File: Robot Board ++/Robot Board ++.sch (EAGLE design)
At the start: 124 parts, among them U10 74XX125.RGY, U11 SCHA4B0400, U12 BLUETOOTH-RN41", U13 XBEE-1XBEE-1_LOCK, U5 TPS5331[8/9].DQP, U6 TPS62082.DSG, U7 PCA9557.RGV, U8 MPU-6050

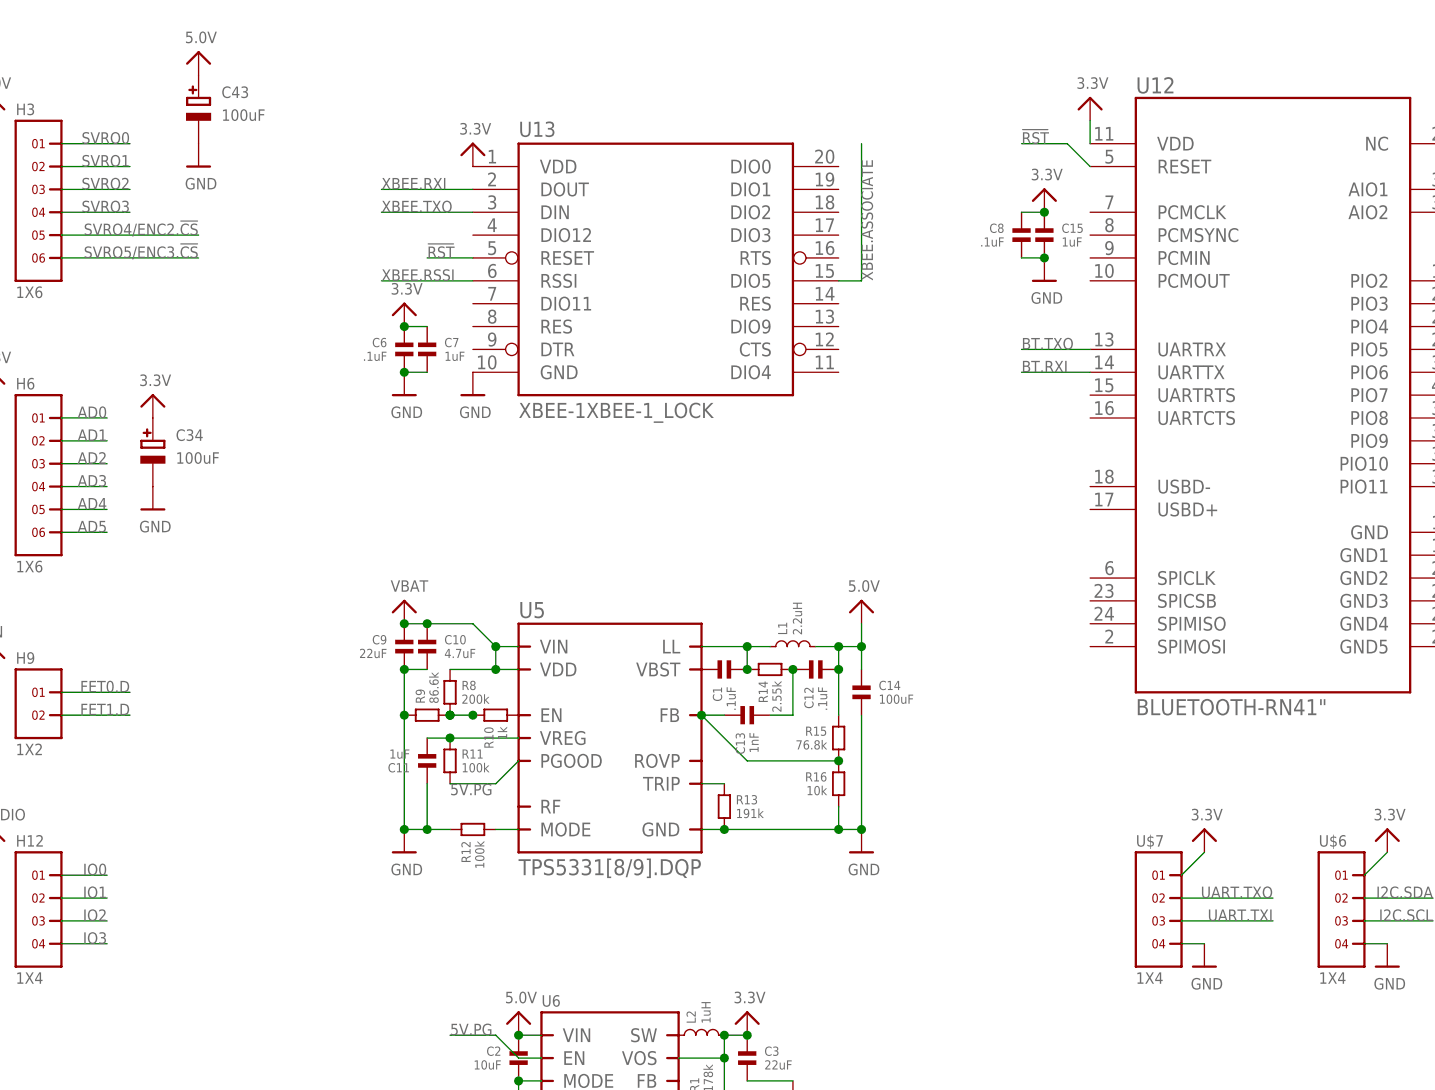
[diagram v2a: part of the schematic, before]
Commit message: Added I2C and UART headers Connected most signals on PCB  Will need to clean up...
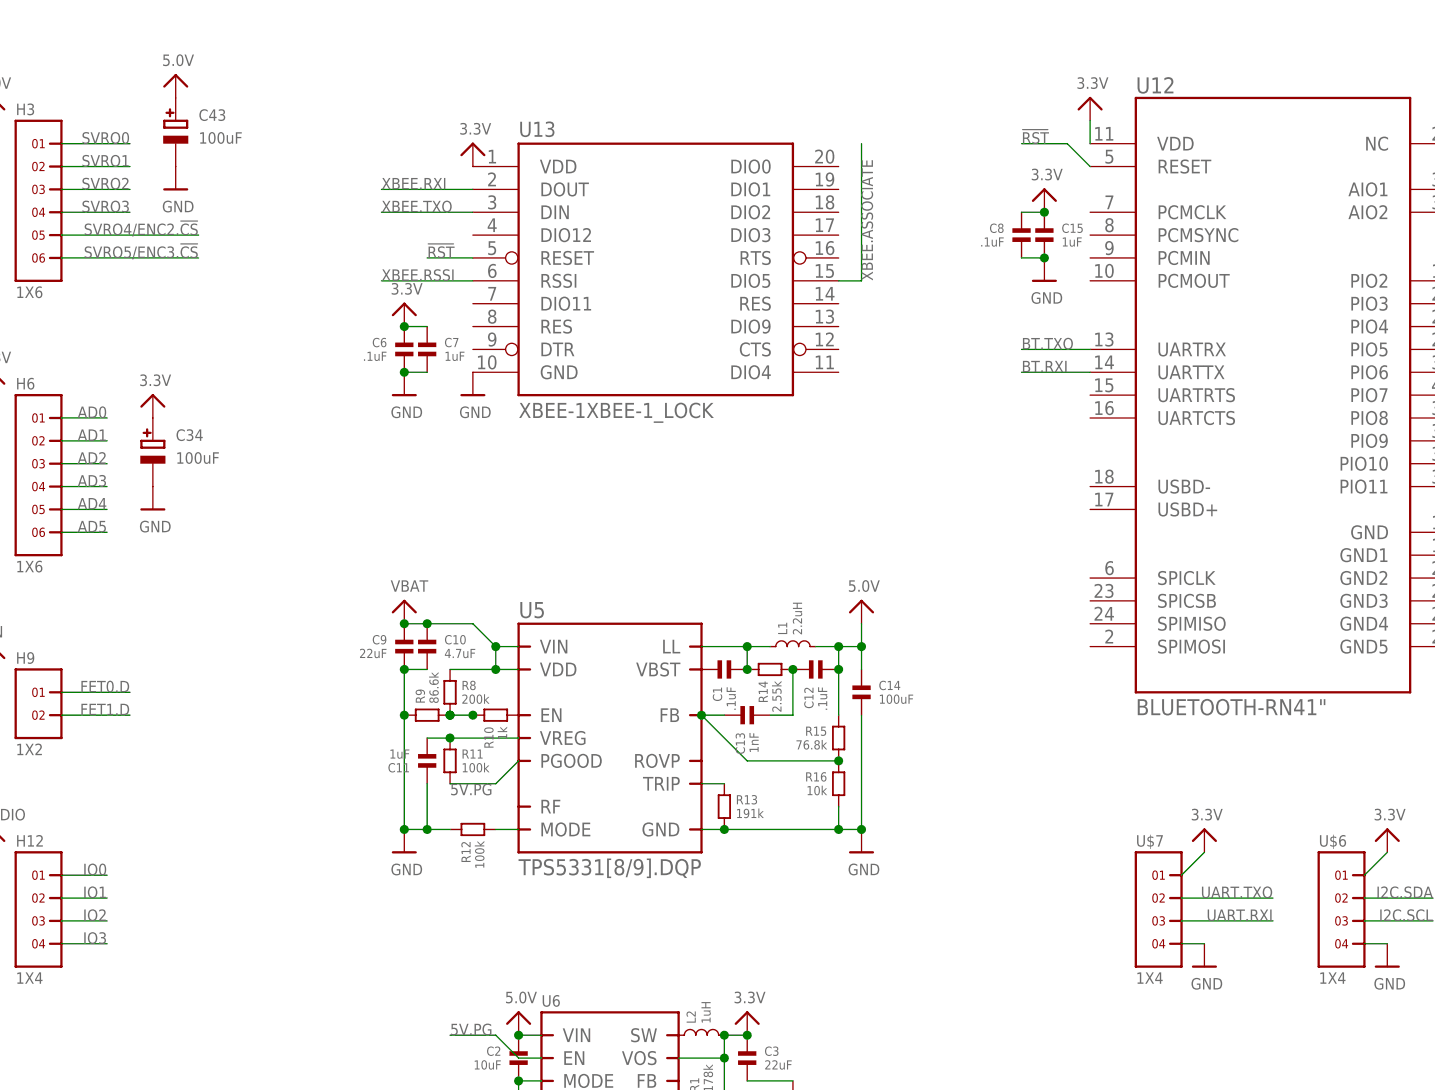
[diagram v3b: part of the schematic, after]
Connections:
- removed net UART.TXI: U$7.3
- net UART.RXI: now also U$7.3
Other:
- moved on the sheet: C43
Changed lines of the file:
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@@
 <instance part="U$138" gate="G$1" x="180.34" y="15.24"/>
 <instance part="U$1" gate="G$1" x="312.42" y="96.52"/>
-<instance part="C43" gate="G$1" x="48.26" y="241.3"/>
-<instance part="U$2" gate="G$1" x="48.26" y="248.92"/>
-<instance part="U$5" gate="G$1" x="48.26" y="236.22"/>
+<instance part="C43" gate="G$1" x="45.72" y="238.76"/>
+<instance part="U$2" gate="G$1" x="45.72" y="246.38"/>
+<instance part="U$5" gate="G$1" x="45.72" y="233.68"/>
 <instance part="U$6" gate="G$1" x="175.26" y="152.4"/>
 <instance part="U$7" gate="G$1" x="154.94" y="152.4"/>
@@
 <label x="289.56" y="195.58" size="1.27" layer="95"/>
 </segment>
+<segment>
+<pinref part="U$7" gate="G$1" pin="3"/>
+<wire x1="167.64" y1="152.4" x2="157.48" y2="152.4" width="0.1524" layer="91"/>
+<label x="167.64" y="152.4" size="1.27" layer="95" rot="MR0"/>
+</segment>
 </net>
 <net name="UART.TXO" class="0">
@@
 </segment>
 </net>
-<net name="UART.TXI" class="0">
-<segment>
-<pinref part="U$7" gate="G$1" pin="3"/>
-<wire x1="167.64" y1="152.4" x2="157.48" y2="152.4" width="0.1524" layer="91"/>
-<label x="167.64" y="152.4" size="1.27" layer="95" rot="MR0"/>
-</segment>
-</net>

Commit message: most power lines routed
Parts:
- removed H25: 1X3, headers(2mm):1X3
- H27: value 1X3 -> 1X2; device headers(2mm):1X3 -> headers(.1in):1X2
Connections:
- net 3.3V: now also H11.1, H11.2, H11.3, H11.4, H13.1, H14.1, H15.1, H16.1; no longer H25.1
- net 5.0V: no longer H25.3, H27.1
- net VBAT: now also H27.2; no longer H27.3
- net VDDIO: no longer H11.1, H11.2, H11.3, H11.4, H13.1, H14.1, H15.1, H16.1, H25.2
- net VIN: now also H27.1; no longer H27.2
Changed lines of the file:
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@@
 <part name="U$72" library="microbuilder" deviceset="3.3V" device=""/>
 <part name="U$74" library="microbuilder" deviceset="GND" device=""/>
-<part name="H25" library="headers(2mm)" deviceset="1X3" device=""/>
-<part name="H27" library="headers(2mm)" deviceset="1X3" device=""/>
-<part name="U$77" library="microbuilder" deviceset="3.3V" device=""/>
-<part name="U$79" library="microbuilder" deviceset="5.0V" device=""/>
-<part name="U$81" library="microbuilder" deviceset="5.0V" device=""/>
+<part name="H27" library="headers(.1in)" deviceset="1X2" device=""/>
 <part name="U$82" library="microbuilder" deviceset="VBAT" device=""/>
 <part name="U$84" library="microbuilder" deviceset="VBAT" device=""/>
@@
 <part name="U$87" library="microbuilder" deviceset="VBAT" device=""/>
 <part name="U$88" library="microbuilder" deviceset="3.3V" device=""/>
-<part name="U$89" library="microbuilder" deviceset="VDDIO" device=""/>
-<part name="U$90" library="microbuilder" deviceset="VDDIO" device=""/>
-<part name="U$51" library="microbuilder" deviceset="VDDIO" device=""/>
-<part name="U$52" library="microbuilder" deviceset="VDDIO" device=""/>
-<part name="U$53" library="microbuilder" deviceset="VDDIO" device=""/>
-<part name="U$54" library="microbuilder" deviceset="VDDIO" device=""/>
 <part name="U$91" library="microbuilder" deviceset="VIN" device=""/>
 <part name="U$92" library="microbuilder" deviceset="VIN" device=""/>
@@
 <part name="U$32" library="microbuilder" deviceset="GND" device=""/>
 <part name="U$30" library="microbuilder" deviceset="3.3V" device=""/>
+<part name="U$33" library="microbuilder" deviceset="3.3V" device=""/>
+<part name="U$35" library="microbuilder" deviceset="3.3V" device=""/>
+<part name="U$36" library="microbuilder" deviceset="3.3V" device=""/>
+<part name="U$37" library="microbuilder" deviceset="3.3V" device=""/>
+<part name="U$38" library="microbuilder" deviceset="3.3V" device=""/>
 </parts>
 <sheets>
@@
 <instance part="U$72" gate="G$1" x="147.32" y="243.84"/>
 <instance part="U$74" gate="G$1" x="205.74" y="208.28"/>
-<instance part="H25" gate="G$1" x="309.88" y="55.88"/>
 <instance part="H27" gate="G$1" x="350.52" y="55.88"/>
-<instance part="U$77" gate="G$1" x="314.96" y="58.42" rot="R270"/>
-<instance part="U$79" gate="G$1" x="314.96" y="53.34" rot="R270"/>
-<instance part="U$81" gate="G$1" x="355.6" y="58.42" rot="R270"/>
 <instance part="U$82" gate="G$1" x="355.6" y="53.34" rot="R270"/>
 <instance part="U$84" gate="G$1" x="55.88" y="68.58" rot="MR0"/>
@@
 <instance part="U$87" gate="G$1" x="71.12" y="68.58"/>
 <instance part="U$88" gate="G$1" x="228.6" y="124.46"/>
-<instance part="U$89" gate="G$1" x="320.04" y="60.96"/>
-<instance part="U$90" gate="G$1" x="25.4" y="162.56"/>
-<instance part="U$51" gate="G$1" x="22.86" y="114.3"/>
-<instance part="U$52" gate="G$1" x="22.86" y="96.52"/>
-<instance part="U$53" gate="G$1" x="63.5" y="96.52"/>
-<instance part="U$54" gate="G$1" x="63.5" y="114.3"/>
-<instance part="U$91" gate="G$1" x="360.68" y="60.96"/>
+<instance part="U$91" gate="G$1" x="355.6" y="58.42"/>
 <instance part="U$92" gate="G$1" x="25.4" y="182.88"/>
 <instance part="U$20" gate="G$1" x="109.22" y="142.24"/>
@@
 <instance part="U$32" gate="G$1" x="43.18" y="198.12"/>
 <instance part="U$30" gate="G$1" x="43.18" y="210.82"/>
+<instance part="U$33" gate="G$1" x="25.4" y="162.56"/>
+<instance part="U$35" gate="G$1" x="22.86" y="114.3"/>
+<instance part="U$36" gate="G$1" x="22.86" y="96.52"/>
+<instance part="U$37" gate="G$1" x="63.5" y="96.52"/>
+<instance part="U$38" gate="G$1" x="63.5" y="114.3"/>
 </instances>
 <busses>
@@
 <net name="3.3V" class="0">
 <segment>
-<pinref part="H25" gate="G$1" pin="1"/>
-<pinref part="U$77" gate="G$1" pin="3.3V"/>
-</segment>
-<segment>
 <pinref part="C3" gate="G$1" pin="1"/>
 <pinref part="U$20" gate="G$1" pin="3.3V"/>
@@
 <pinref part="U$30" gate="G$1" pin="3.3V"/>
 </segment>
+<segment>
+<pinref part="H11" gate="G$1" pin="4"/>
+<wire x1="25.4" y1="149.86" x2="25.4" y2="152.4" width="0.1524" layer="91"/>
+<pinref part="H11" gate="G$1" pin="3"/>
+<junction x="25.4" y="152.4"/>
+<wire x1="25.4" y1="152.4" x2="25.4" y2="154.94" width="0.1524" layer="91"/>
+<pinref part="H11" gate="G$1" pin="2"/>
+<junction x="25.4" y="154.94"/>
+<wire x1="25.4" y1="154.94" x2="25.4" y2="157.48" width="0.1524" layer="91"/>
+<pinref part="H11" gate="G$1" pin="1"/>
+<junction x="25.4" y="157.48"/>
+<wire x1="25.4" y1="157.48" x2="25.4" y2="160.02" width="0.1524" layer="91"/>
+<pinref part="U$33" gate="G$1" pin="3.3V"/>
+</segment>
+<segment>
+<pinref part="H13" gate="G$1" pin="1"/>
+<wire x1="22.86" y1="111.76" x2="25.4" y2="109.22" width="0.1524" layer="91"/>
+<pinref part="U$35" gate="G$1" pin="3.3V"/>
+</segment>
+<segment>
+<pinref part="H14" gate="G$1" pin="1"/>
+<wire x1="22.86" y1="93.98" x2="25.4" y2="91.44" width="0.1524" layer="91"/>
+<pinref part="U$36" gate="G$1" pin="3.3V"/>
+</segment>
+<segment>
+<pinref part="H16" gate="G$1" pin="1"/>
+<wire x1="63.5" y1="93.98" x2="66.04" y2="91.44" width="0.1524" layer="91"/>
+<pinref part="U$37" gate="G$1" pin="3.3V"/>
+</segment>
+<segment>
+<pinref part="H15" gate="G$1" pin="1"/>
+<wire x1="63.5" y1="111.76" x2="66.04" y2="109.22" width="0.1524" layer="91"/>
+<pinref part="U$38" gate="G$1" pin="3.3V"/>
+</segment>
 </net>
 <net name="SVRO0" class="0">
@@
 <segment>
 <pinref part="U7" gate="G$1" pin="P4"/>
-<wire x1="177.8" y1="86.36" x2="182.88" y2="86.36" width="0.1524" layer="91"/>
-<label x="182.88" y="86.36" size="1.27" layer="95" rot="MR0"/>
+<wire x1="177.8" y1="86.36" x2="185.42" y2="86.36" width="0.1524" layer="91"/>
+<label x="185.42" y="86.36" size="1.27" layer="95" rot="MR0"/>
 </segment>
 </net>
@@
 <segment>
 <pinref part="U7" gate="G$1" pin="P5"/>
-<wire x1="177.8" y1="83.82" x2="182.88" y2="83.82" width="0.1524" layer="91"/>
-<label x="182.88" y="83.82" size="1.27" layer="95" rot="MR0"/>
+<wire x1="177.8" y1="83.82" x2="185.42" y2="83.82" width="0.1524" layer="91"/>
+<label x="185.42" y="83.82" size="1.27" layer="95" rot="MR0"/>
 </segment>
 </net>
@@
 </segment>
 <segment>
-<pinref part="H25" gate="G$1" pin="3"/>
-<pinref part="U$79" gate="G$1" pin="5.0V"/>
-</segment>
-<segment>
-<pinref part="H27" gate="G$1" pin="1"/>
-<pinref part="U$81" gate="G$1" pin="5.0V"/>
-</segment>
-<segment>
 <pinref part="L1" gate="G$1" pin="2"/>
 <wire x1="116.84" y1="182.88" x2="119.38" y2="182.88" width="0.1524" layer="91"/>
@@
 <net name="VBAT" class="0">
 <segment>
-<pinref part="H27" gate="G$1" pin="3"/>
+<pinref part="H27" gate="G$1" pin="2"/>
 <pinref part="U$82" gate="G$1" pin="VBAT"/>
 </segment>
@@
 <net name="VDDIO" class="0">
 <segment>
-<pinref part="H25" gate="G$1" pin="2"/>
-<wire x1="312.42" y1="55.88" x2="320.04" y2="55.88" width="0.1524" layer="91"/>
-<pinref part="U$89" gate="G$1" pin="VDDIO"/>
-<wire x1="320.04" y1="55.88" x2="320.04" y2="58.42" width="0.1524" layer="91"/>
-</segment>
-<segment>
-<pinref part="U$90" gate="G$1" pin="VDDIO"/>
-<pinref part="H11" gate="G$1" pin="4"/>
-<wire x1="25.4" y1="149.86" x2="25.4" y2="152.4" width="0.1524" layer="91"/>
-<pinref part="H11" gate="G$1" pin="3"/>
-<junction x="25.4" y="152.4"/>
-<wire x1="25.4" y1="152.4" x2="25.4" y2="154.94" width="0.1524" layer="91"/>
-<pinref part="H11" gate="G$1" pin="2"/>
-<junction x="25.4" y="154.94"/>
-<wire x1="25.4" y1="154.94" x2="25.4" y2="157.48" width="0.1524" layer="91"/>
-<pinref part="H11" gate="G$1" pin="1"/>
-<junction x="25.4" y="157.48"/>
-<wire x1="25.4" y1="157.48" x2="25.4" y2="160.02" width="0.1524" layer="91"/>
-</segment>
-<segment>
-<pinref part="H13" gate="G$1" pin="1"/>
-<pinref part="U$51" gate="G$1" pin="VDDIO"/>
-<wire x1="22.86" y1="111.76" x2="25.4" y2="109.22" width="0.1524" layer="91"/>
-</segment>
-<segment>
-<pinref part="H14" gate="G$1" pin="1"/>
-<pinref part="U$52" gate="G$1" pin="VDDIO"/>
-<wire x1="22.86" y1="93.98" x2="25.4" y2="91.44" width="0.1524" layer="91"/>
-</segment>
-<segment>
-<pinref part="H16" gate="G$1" pin="1"/>
-<pinref part="U$53" gate="G$1" pin="VDDIO"/>
-<wire x1="63.5" y1="93.98" x2="66.04" y2="91.44" width="0.1524" layer="91"/>
-</segment>
-<segment>
-<pinref part="H15" gate="G$1" pin="1"/>
-<pinref part="U$54" gate="G$1" pin="VDDIO"/>
-<wire x1="63.5" y1="111.76" x2="66.04" y2="109.22" width="0.1524" layer="91"/>
-</segment>
-<segment>
 <pinref part="R5" gate="G$1" pin="1"/>
 <pinref part="U$58" gate="G$1" pin="VDDIO"/>
@@
 </segment>
 <segment>
-<pinref part="H27" gate="G$1" pin="2"/>
-<wire x1="353.06" y1="55.88" x2="360.68" y2="55.88" width="0.1524" layer="91"/>
+<pinref part="H27" gate="G$1" pin="1"/>
+<wire x1="353.06" y1="55.88" x2="355.6" y2="55.88" width="0.1524" layer="91"/>
 <pinref part="U$91" gate="G$1" pin="VIN"/>
-<wire x1="360.68" y1="58.42" x2="360.68" y2="55.88" width="0.1524" layer="91"/>
-</segment>
-</net>
+</segment>
+</net>

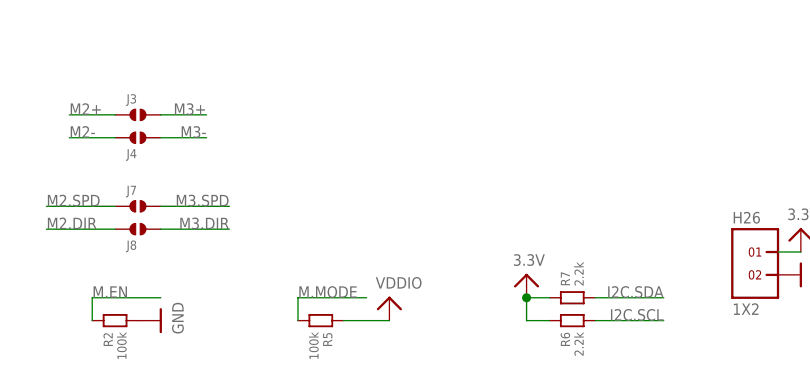
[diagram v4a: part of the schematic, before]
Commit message: More routing. Most motor control signals completed. Successfully making larger ground plane.
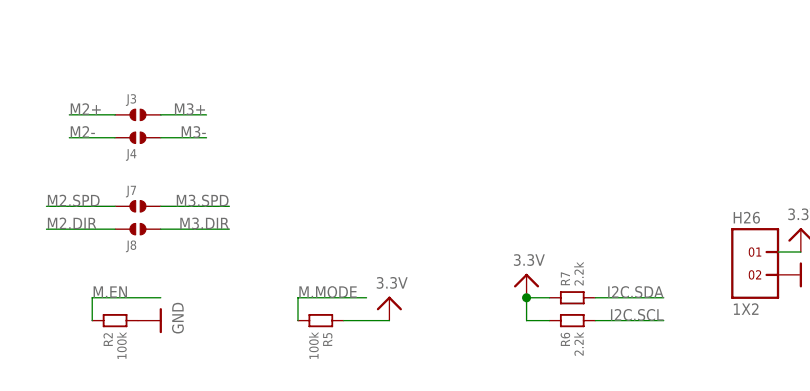
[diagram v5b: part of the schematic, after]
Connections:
- removed net VDDIO: R5.1
- net 3.3V: now also R5.1
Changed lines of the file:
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@@
 <part name="U$56" library="microbuilder" deviceset="GND" device=""/>
 <part name="R5" library="standardparts" deviceset="RESISTOR" device=".0603" value="100k"/>
-<part name="U$58" library="microbuilder" deviceset="VDDIO" device=""/>
 <part name="U$111" library="microbuilder" deviceset="3.3V" device=""/>
 <part name="U$137" library="microbuilder" deviceset="GND" device=""/>
@@
 <part name="U$37" library="microbuilder" deviceset="3.3V" device=""/>
 <part name="U$38" library="microbuilder" deviceset="3.3V" device=""/>
+<part name="U$39" library="microbuilder" deviceset="3.3V" device=""/>
 </parts>
 <sheets>
@@
 <instance part="U$56" gate="G$1" x="347.98" y="88.9"/>
 <instance part="R5" gate="G$1" x="157.48" y="10.16" rot="R180"/>
-<instance part="U$58" gate="G$1" x="165.1" y="12.7"/>
 <instance part="U$111" gate="G$1" x="340.36" y="198.12"/>
 <instance part="U$137" gate="G$1" x="340.36" y="187.96"/>
@@
 <instance part="U$37" gate="G$1" x="63.5" y="96.52"/>
 <instance part="U$38" gate="G$1" x="63.5" y="114.3"/>
+<instance part="U$39" gate="G$1" x="165.1" y="12.7"/>
 </instances>
 <busses>
@@
 <pinref part="U$38" gate="G$1" pin="3.3V"/>
 </segment>
+<segment>
+<pinref part="R5" gate="G$1" pin="1"/>
+<wire x1="160.02" y1="10.16" x2="165.1" y2="10.16" width="0.1524" layer="91"/>
+<pinref part="U$39" gate="G$1" pin="3.3V"/>
+</segment>
 </net>
 <net name="SVRO0" class="0">
@@
 </segment>
 </net>
-<net name="VDDIO" class="0">
-<segment>
-<pinref part="R5" gate="G$1" pin="1"/>
-<pinref part="U$58" gate="G$1" pin="VDDIO"/>
-<wire x1="160.02" y1="10.16" x2="165.1" y2="10.16" width="0.1524" layer="91"/>
-</segment>
-</net>

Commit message: No airwires left!!! ^_^
Time for a nap...
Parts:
- U10: value 74XX125.RGY -> 74LVTH125.RGY
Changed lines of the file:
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@@
 <part name="LED3" library="standardparts" deviceset="LED" device=".0603"/>
 <part name="H23" library="headers(2mm)" deviceset="2X3" device=""/>
-<part name="U10" library="packages(ti)" deviceset="74XX125" device=".RGY"/>
+<part name="U10" library="packages(ti)" deviceset="74XX125" device=".RGY" value="74LVTH125.RGY"/>
 <part name="U$133" library="microbuilder" deviceset="3.3V" device=""/>
 <part name="U$134" library="microbuilder" deviceset="GND" device=""/>
